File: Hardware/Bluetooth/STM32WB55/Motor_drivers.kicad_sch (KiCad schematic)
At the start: 8 parts, among them IC3 ZXBM5210-SP-13, IC4 ZXBM5210-SP-13

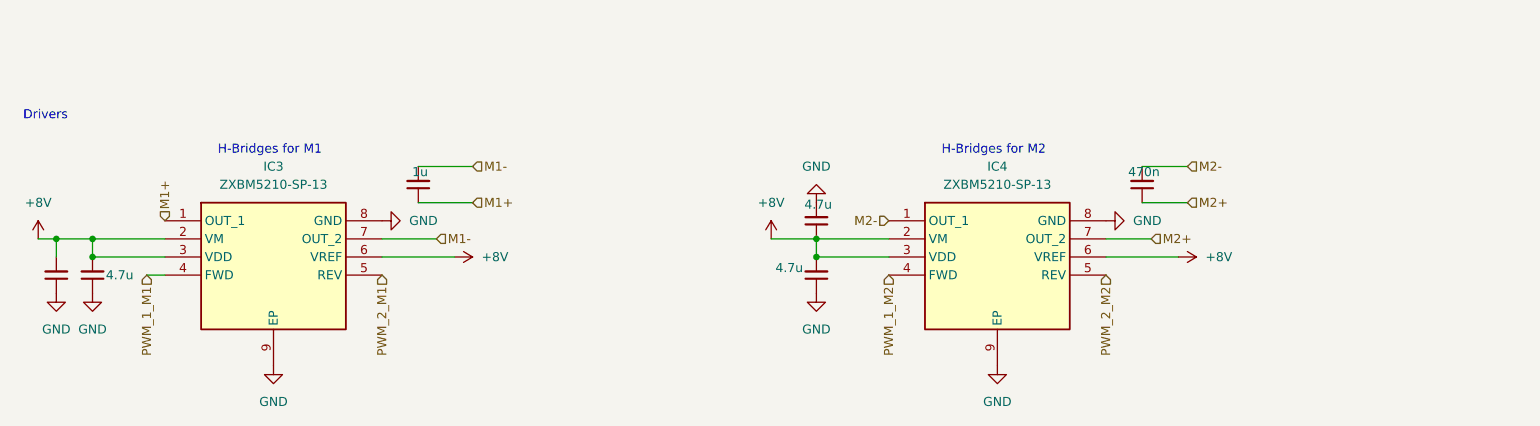
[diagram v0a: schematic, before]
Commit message: schematic update
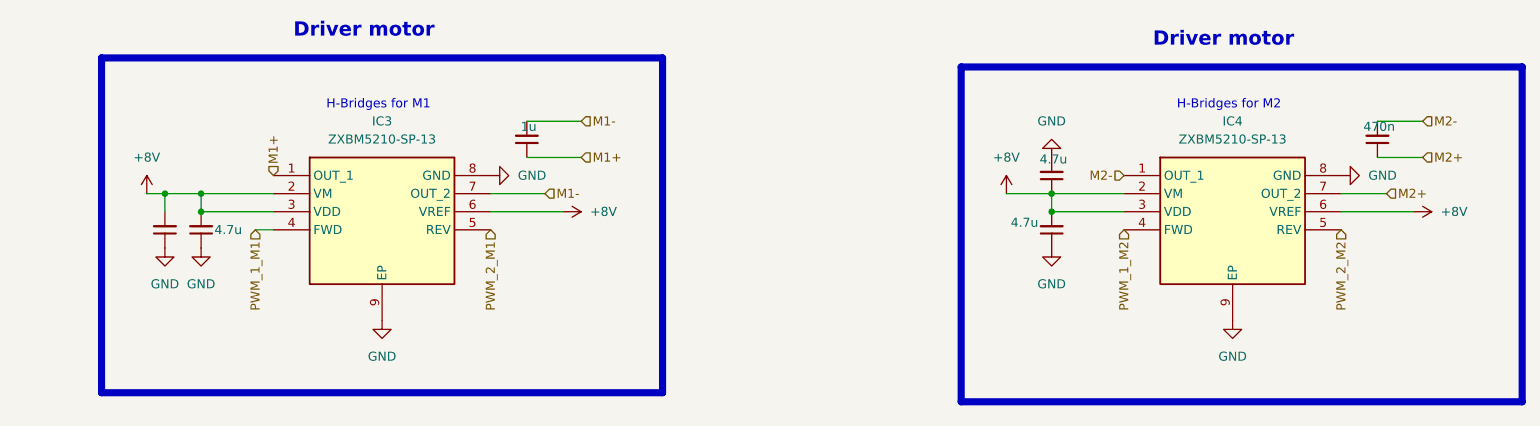
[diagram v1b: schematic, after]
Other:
- note added: "Driver motor"
- note removed: "Drivers"
- moved on the sheet: IC3, IC4
